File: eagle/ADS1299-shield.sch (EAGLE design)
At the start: 118 parts, among them IC1 24AA256UID, IC2 TPS72325DBVT, IC3 TPS73225DBVT, J8 Electrode Connector, U1 ADS1299IPAG, U2 TXB0108PWR, U3 TXB0108PWR

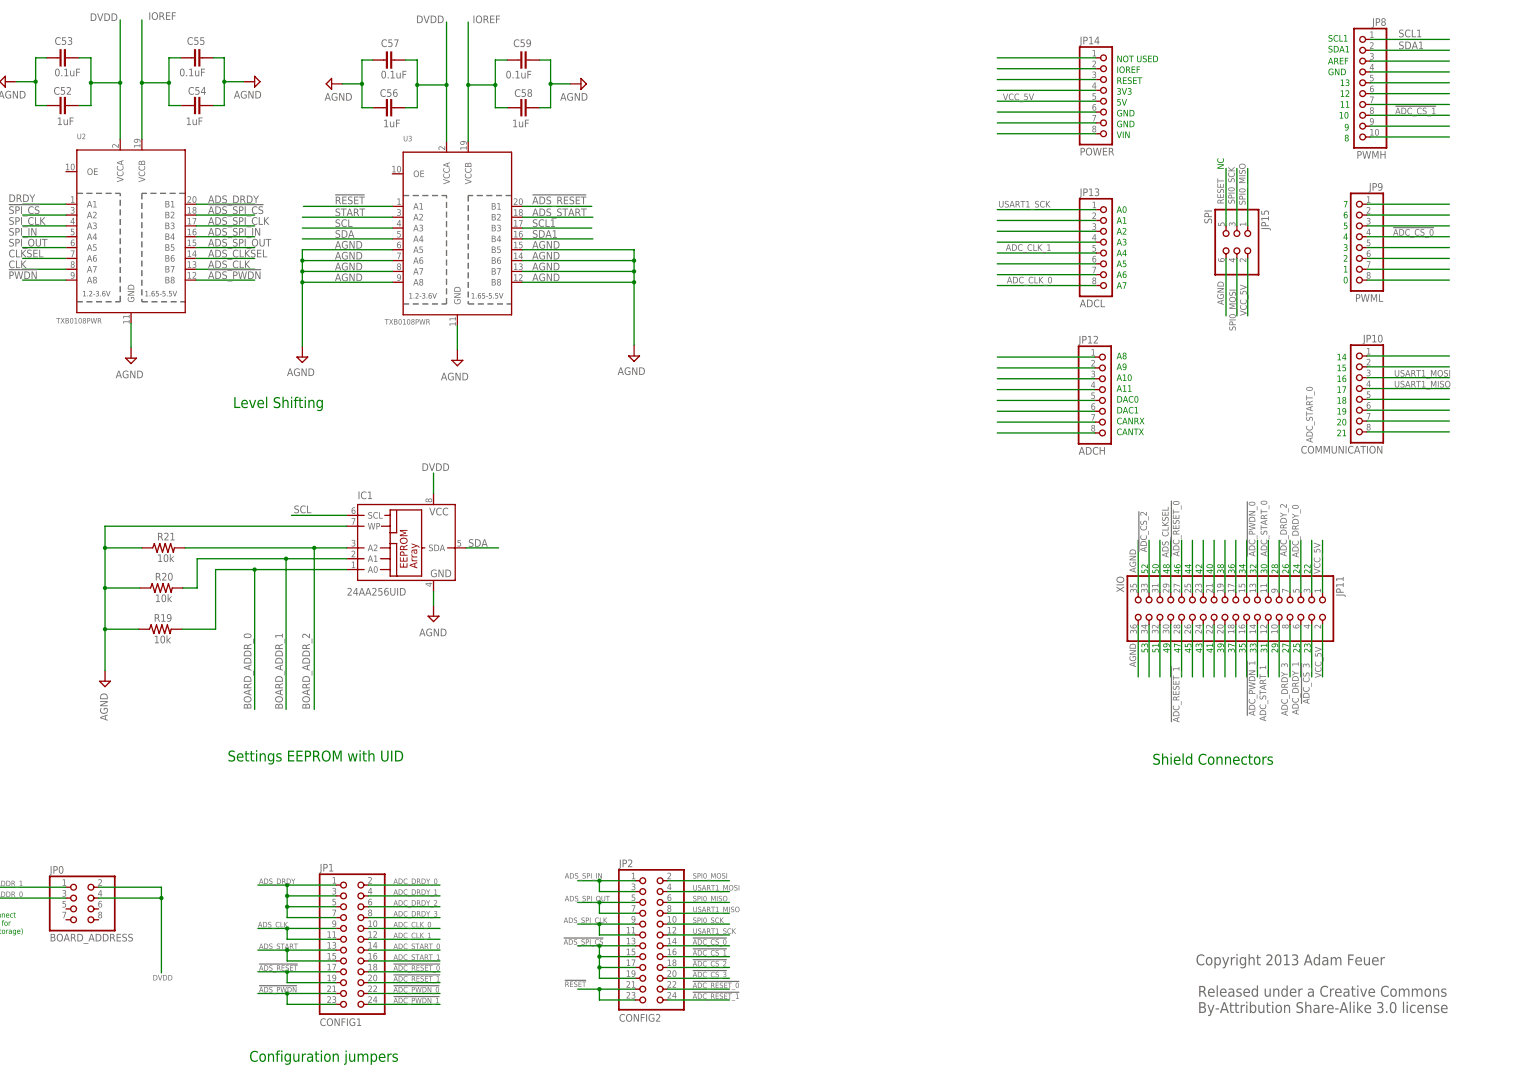
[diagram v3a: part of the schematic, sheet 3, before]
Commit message: added test points for power; added fiducials; partially grouped AIN block passives, EEPROM resistors, and level shifter decoupling caps
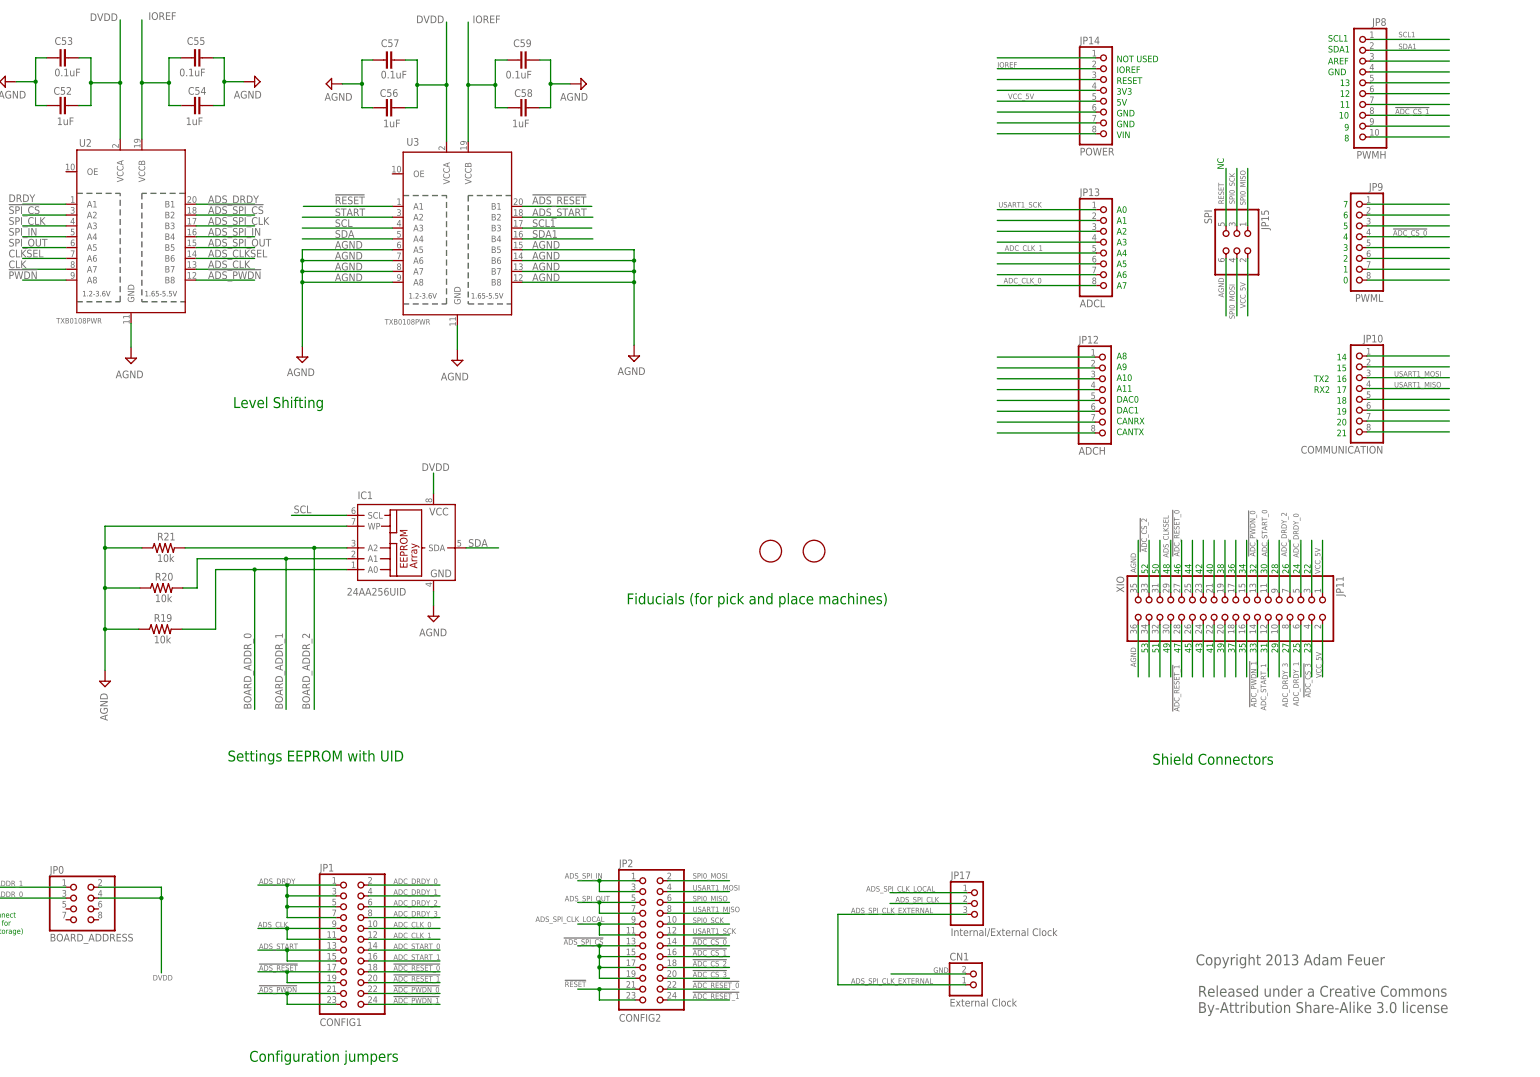
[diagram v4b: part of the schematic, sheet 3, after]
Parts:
- added CN1: External Clock, adafruit:JST_2PIN-SMT-RA
- added JP16: AVDD_TEST_POINT, adafruit:PINHD-1X1
- added JP17: Internal/External Clock, adafruit:PINHD-1X3
- added JP18: AVSS_TEST_POINT, adafruit:PINHD-1X1
- added U$5, U$6: FIDUCIAL, adafruit:FIDUCIAL
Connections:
- removed net N$68: JP14.2
- new net ADS_SPI_CLK_EXTERNAL: CN1.2, JP17.3
- new net ADS_SPI_CLK_LOCAL: JP17.1, JP2.11, JP2.9
- net ADS_SPI_CLK: now also JP17.2; no longer JP2.11, JP2.9
- net AIN1N: now also R3.2; no longer R2.2
- net AIN1P: now also R2.2; no longer R3.2
- net AVDD: now also JP16.1
- net AVSS: now also JP18.1
- net GND: now also CN1.1
- net IN1N: now also R3.1; no longer R2.1
- net IN1P: now also R2.1; no longer R3.1
- net IOREF: now also JP14.2
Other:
- note added: "Fiducials (for pick and place machines)"
- note added: "RX2"
- note added: "Stimulus-Response Buffer (SRB)"
- note added: "TX2"
- note removed: "SRB"
- moved on the sheet: R2, R3

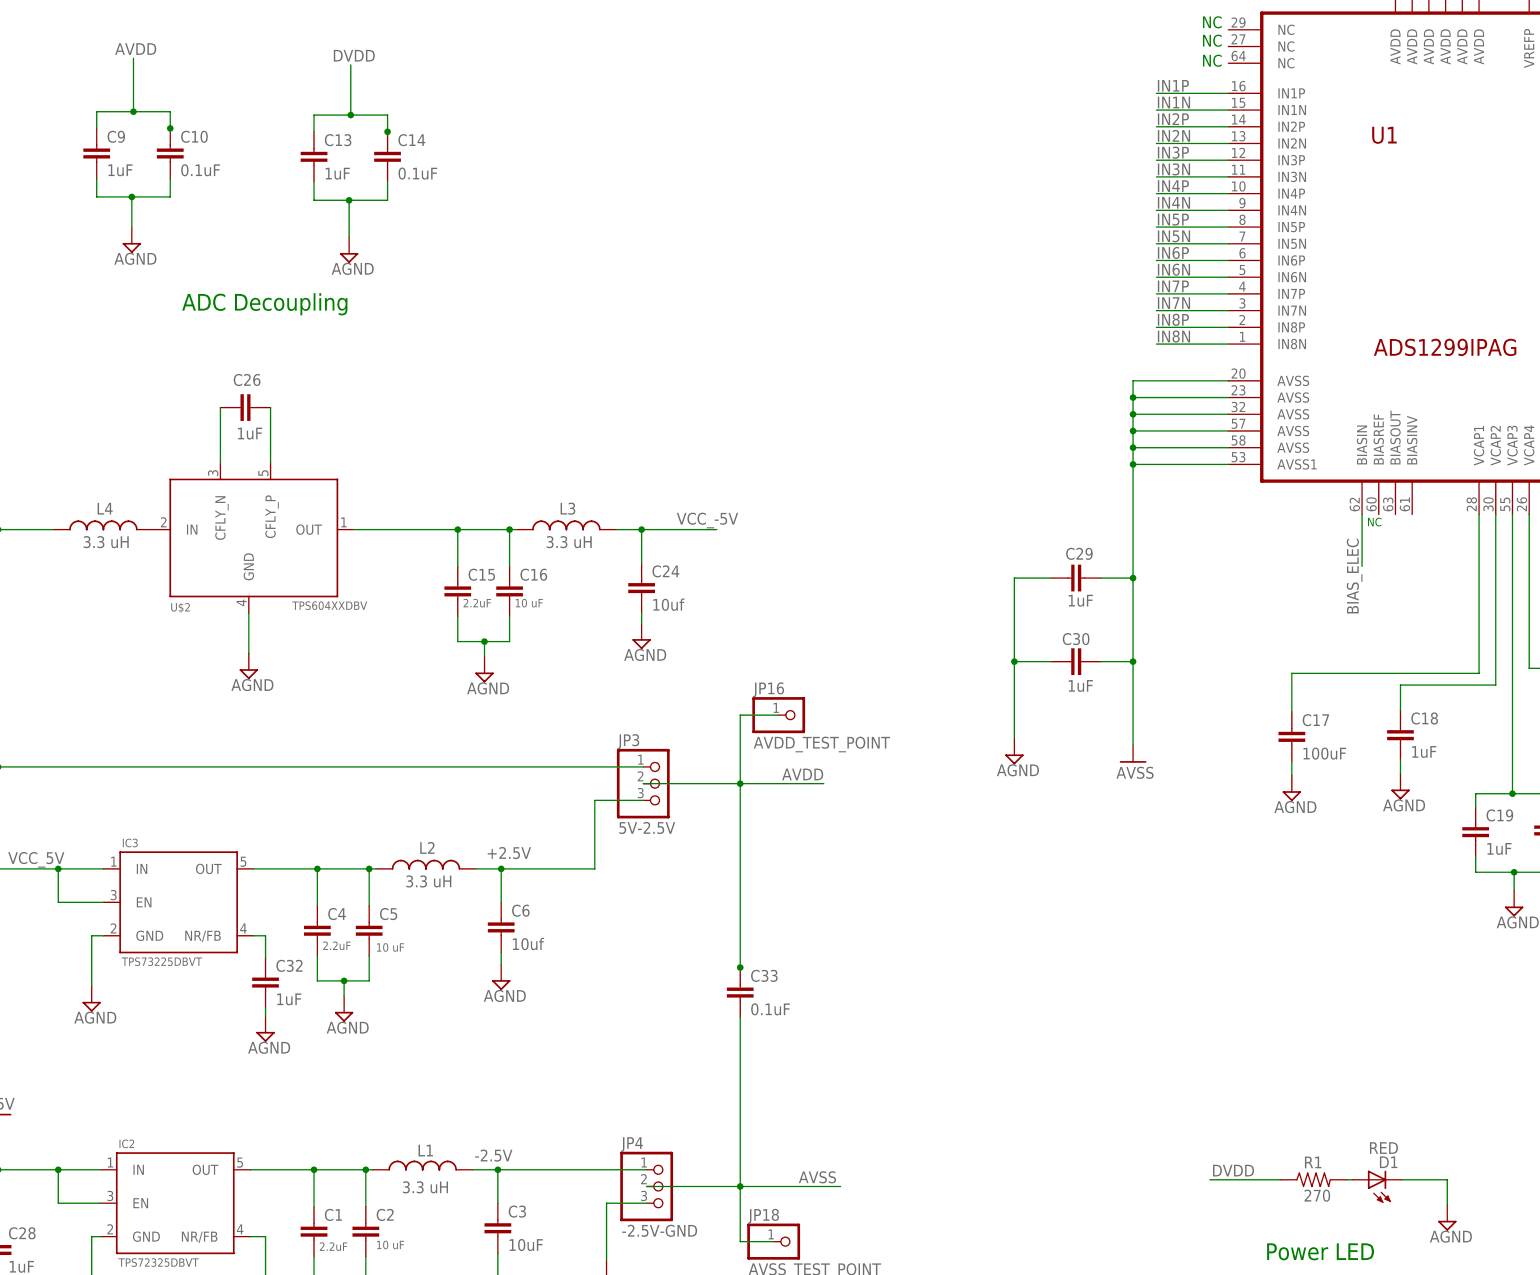
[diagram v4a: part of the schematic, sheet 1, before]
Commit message: grouped positive and negative power components
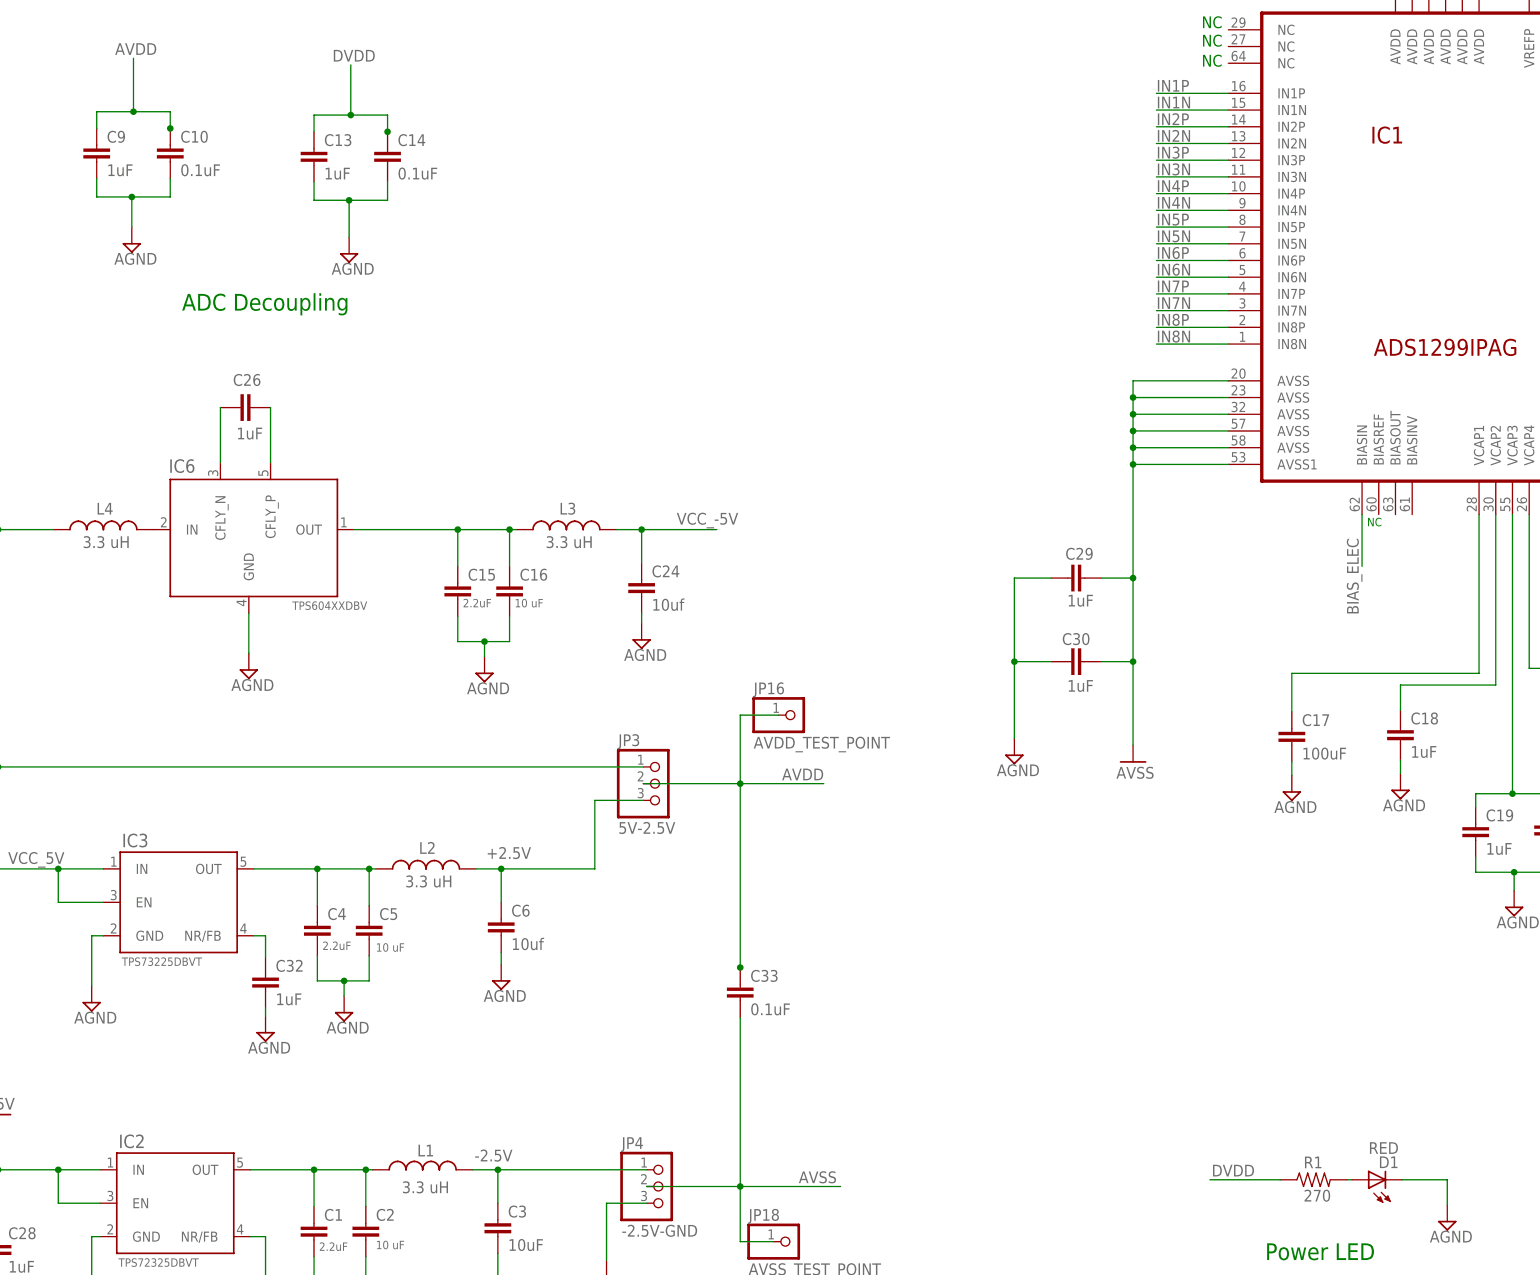
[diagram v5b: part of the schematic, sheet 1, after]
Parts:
- removed U1: ADS1299IPAG, ADS129x:ADS1299*PAG*
- added IC5: 24AA256UID, microchip:24LC256SN
- IC1: value 24AA256UID -> ADS1299IPAG; device microchip:24LC256SN -> ADS129x:ADS1299*PAG*
- renumbered U$2 to IC6, U$3 to IC8, U$4 to IC7
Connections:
- net !PWDN: now also IC1.!PWDN; no longer U1.!PWDN
- net !RESET: now also IC1.!RESET; no longer U1.!RESET
- net !SPI_CS: now also IC1.!CS; no longer U1.!CS
- net AGND: now also IC1.DAISY_IN, IC1.DGND@1, IC1.DGND@2, IC1.DGND@3, IC1.VREFN, IC5.GND, IC5.WP; no longer IC1.GND, IC1.WP, U1.DAISY_IN, U1.DGND@1, U1.DGND@2, U1.DGND@3, U1.VREFN
- net AVDD: now also IC1.AVDD@1, IC1.AVDD@2, IC1.AVDD@3, IC1.AVDD@4, IC1.AVDD@5, IC1.AVDD@6; no longer U1.AVDD@1, U1.AVDD@2, U1.AVDD@3, U1.AVDD@4, U1.AVDD@5, U1.AVDD@6
- net AVSS: now also IC1.AVSS1, IC1.AVSS@1, IC1.AVSS@2, IC1.AVSS@3, IC1.AVSS@4, IC1.AVSS@5; no longer U1.AVSS1, U1.AVSS@1, U1.AVSS@2, U1.AVSS@3, U1.AVSS@4, U1.AVSS@5
- net BIAS_ELEC: now also IC1.BIASIN; no longer U1.BIASIN
- net BOARD_ADDR_0: now also IC1.GPIO1, IC5.A0; no longer IC1.A0, U1.GPIO1
- net BOARD_ADDR_1: now also IC1.GPIO2, IC5.A1; no longer IC1.A1, U1.GPIO2
- net BOARD_ADDR_2: now also IC1.GPIO3, IC5.A2; no longer IC1.A2, U1.GPIO3
- net CLK: now also IC1.CLK; no longer U1.CLK
- net CLKSEL: now also IC1.CLKSEL; no longer U1.CLKSEL
- net DRDY: now also IC1.!DRDY; no longer U1.!DRDY
- net DVDD: now also IC1.DVDD@1, IC1.DVDD@2, IC5.VCC; no longer IC1.VCC, U1.DVDD@1, U1.DVDD@2
- net GPIO4: now also IC1.GPIO4; no longer U1.GPIO4
- net IN1N: now also IC1.IN1N; no longer U1.IN1N
- net IN1P: now also IC1.IN1P; no longer U1.IN1P
- net IN2N: now also IC1.IN2N; no longer U1.IN2N
- net IN2P: now also IC1.IN2P; no longer U1.IN2P
- net IN3N: now also IC1.IN3N; no longer U1.IN3N
- net IN3P: now also IC1.IN3P; no longer U1.IN3P
- net IN4N: now also IC1.IN4N; no longer U1.IN4N
- net IN4P: now also IC1.IN4P; no longer U1.IN4P
- net IN5N: now also IC1.IN5N; no longer U1.IN5N
- net IN5P: now also IC1.IN5P; no longer U1.IN5P
- net IN6N: now also IC1.IN6N; no longer U1.IN6N
- net IN6P: now also IC1.IN6P; no longer U1.IN6P
- net IN7N: now also IC1.IN7N; no longer U1.IN7N
- net IN7P: now also IC1.IN7P; no longer U1.IN7P
- net IN8N: now also IC1.IN8N; no longer U1.IN8N
- net IN8P: now also IC1.IN8P; no longer U1.IN8P
- net N$3: now also IC1.VCAP1; no longer U1.VCAP1
- net N$4: now also IC1.VCAP2; no longer U1.VCAP2
- net N$5: now also IC1.VCAP3; no longer U1.VCAP3
- net N$8: now also IC1.VCAP4; no longer U1.VCAP4
- net SCL: now also IC5.SCL; no longer IC1.SCL
- net SDA: now also IC5.SDA; no longer IC1.SDA
- net SPI_CLK: now also IC1.SCLK; no longer U1.SCLK
- net SPI_IN: now also IC1.DIN; no longer U1.DIN
- net SPI_OUT: now also IC1.DOUT; no longer U1.DOUT
- net SRB1: now also IC1.SRB2; no longer U1.SRB2
- net SRB2: now also IC1.SRB1; no longer U1.SRB1
- net START: now also IC1.START; no longer U1.START
- net VREFP: now also IC1.VREFP; no longer U1.VREFP
